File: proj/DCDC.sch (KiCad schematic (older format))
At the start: 49 parts, among them Q13 MMBT3904, Q15 MMBT3904, Q16 MMBT3904, Q17 PZT2907A, Q18 PZT2907A, Q19 MMBT3904, U14 L78M05CDT, U15 MC79M05CDT, U16 AZ1117CH-1.8TRG1, U17 MCP1700T-vv02E/TT

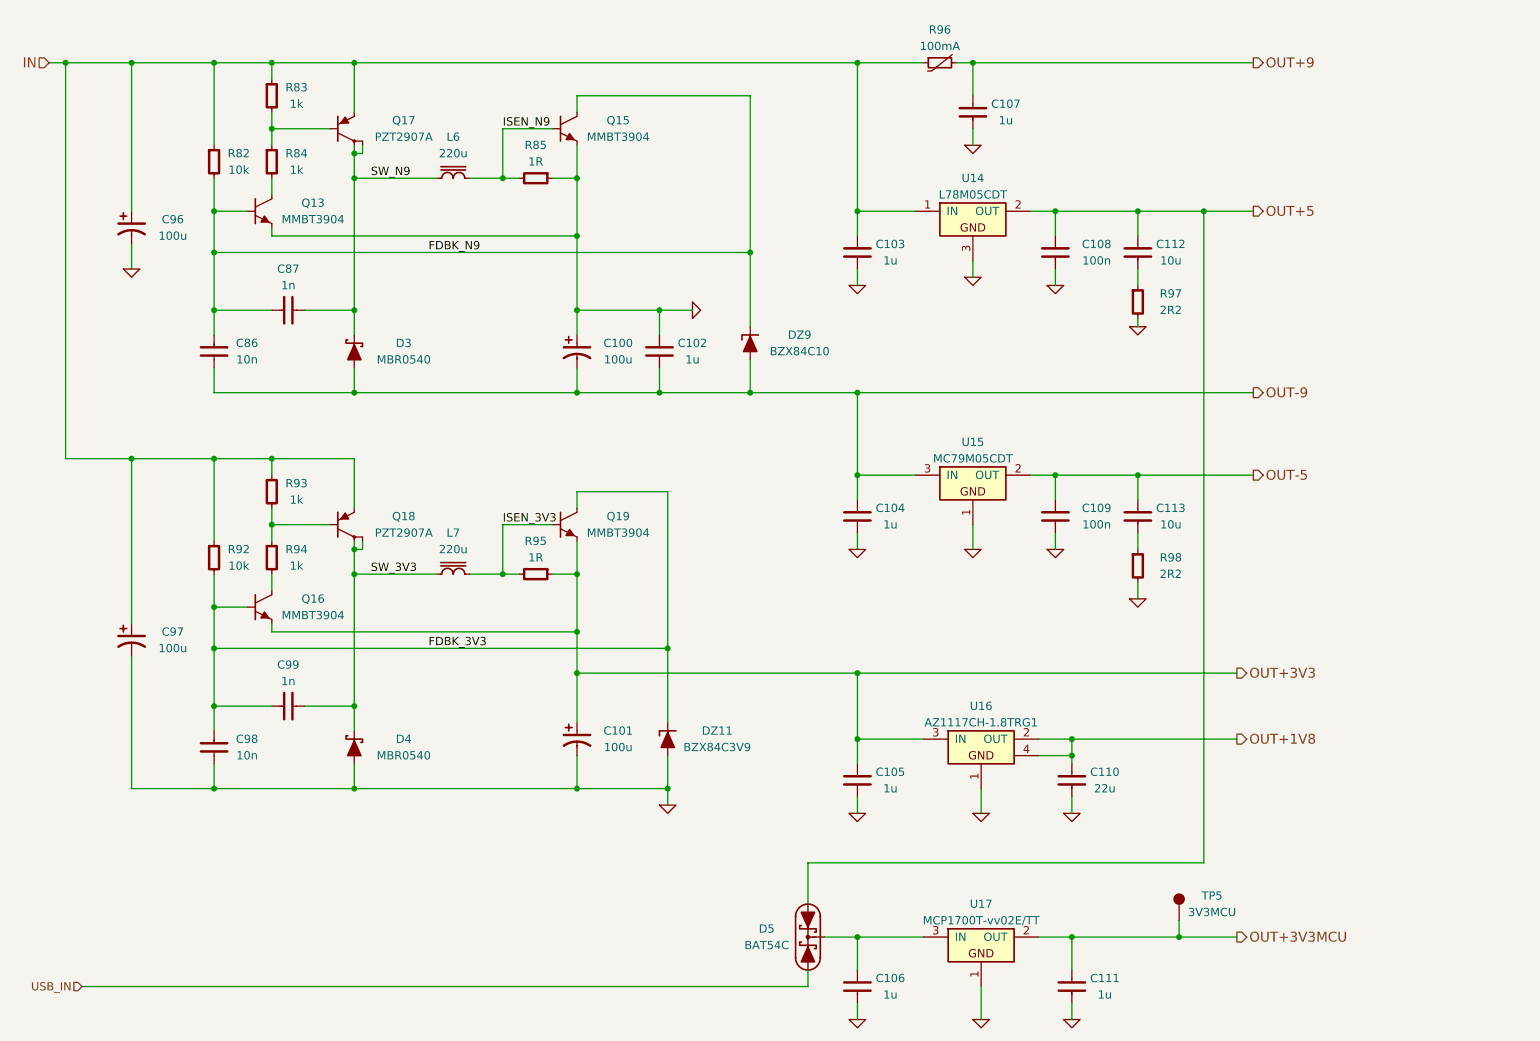
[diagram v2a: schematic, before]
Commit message: Add overload protection to aux power output
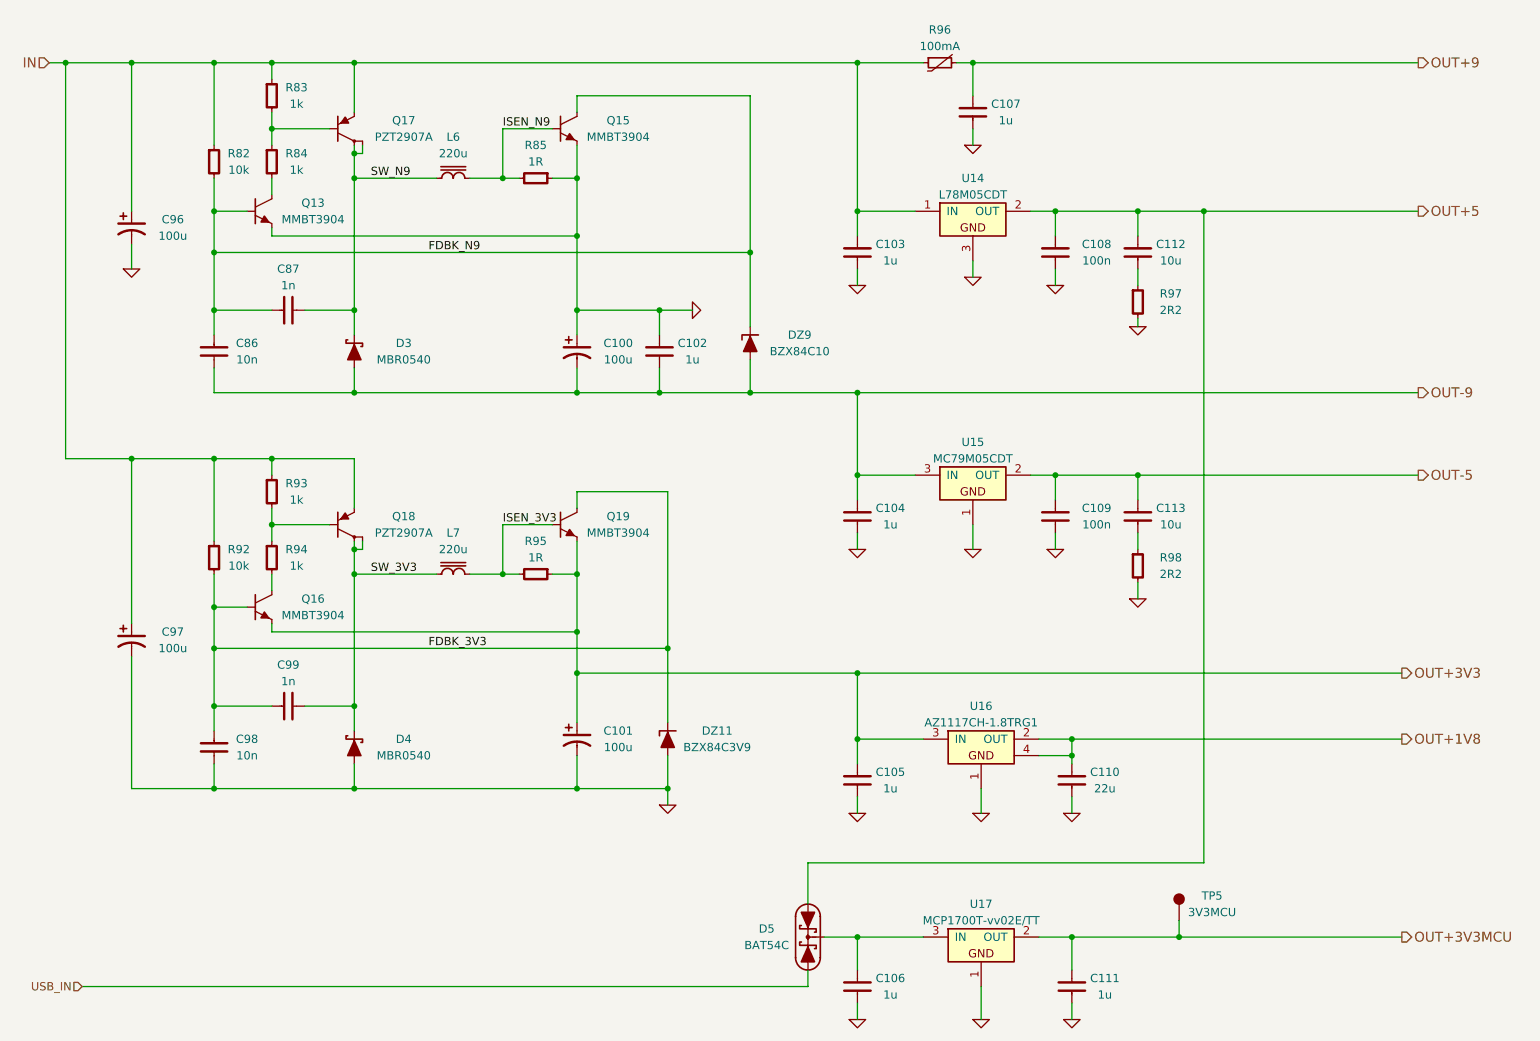
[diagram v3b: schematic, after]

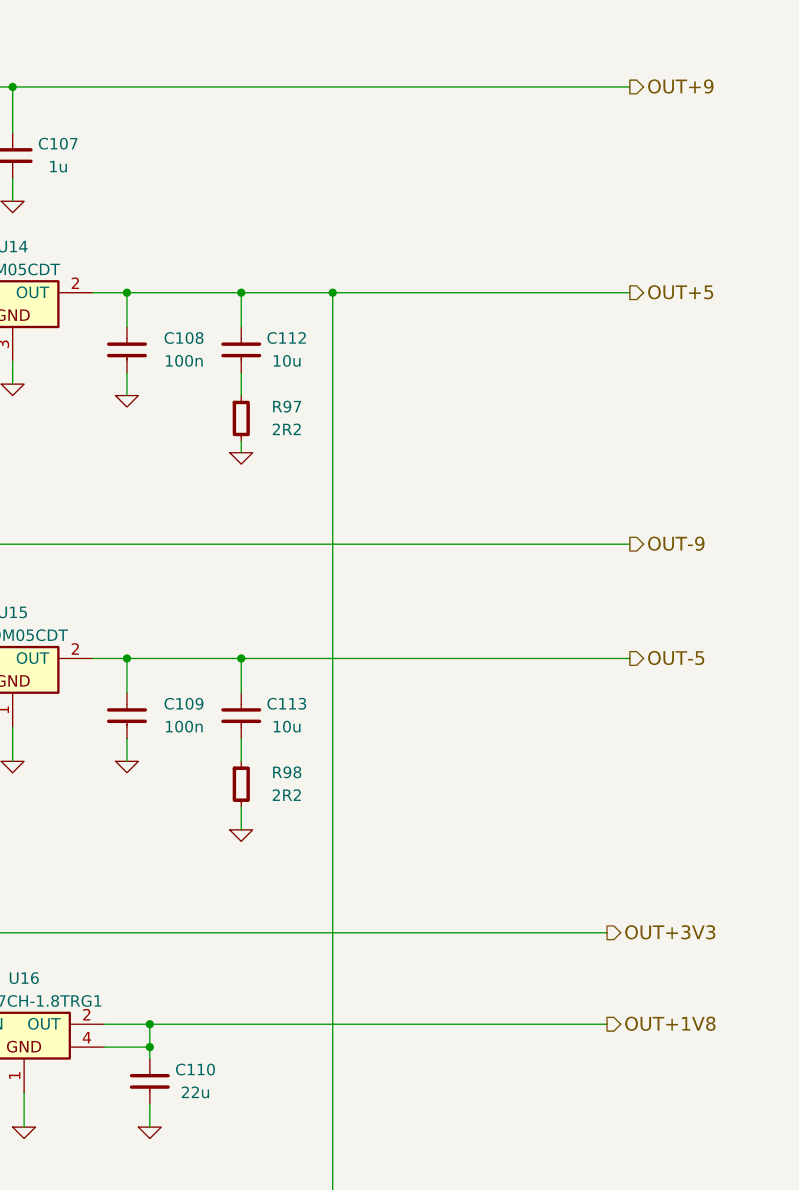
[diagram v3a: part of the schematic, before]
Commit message: Add some test points
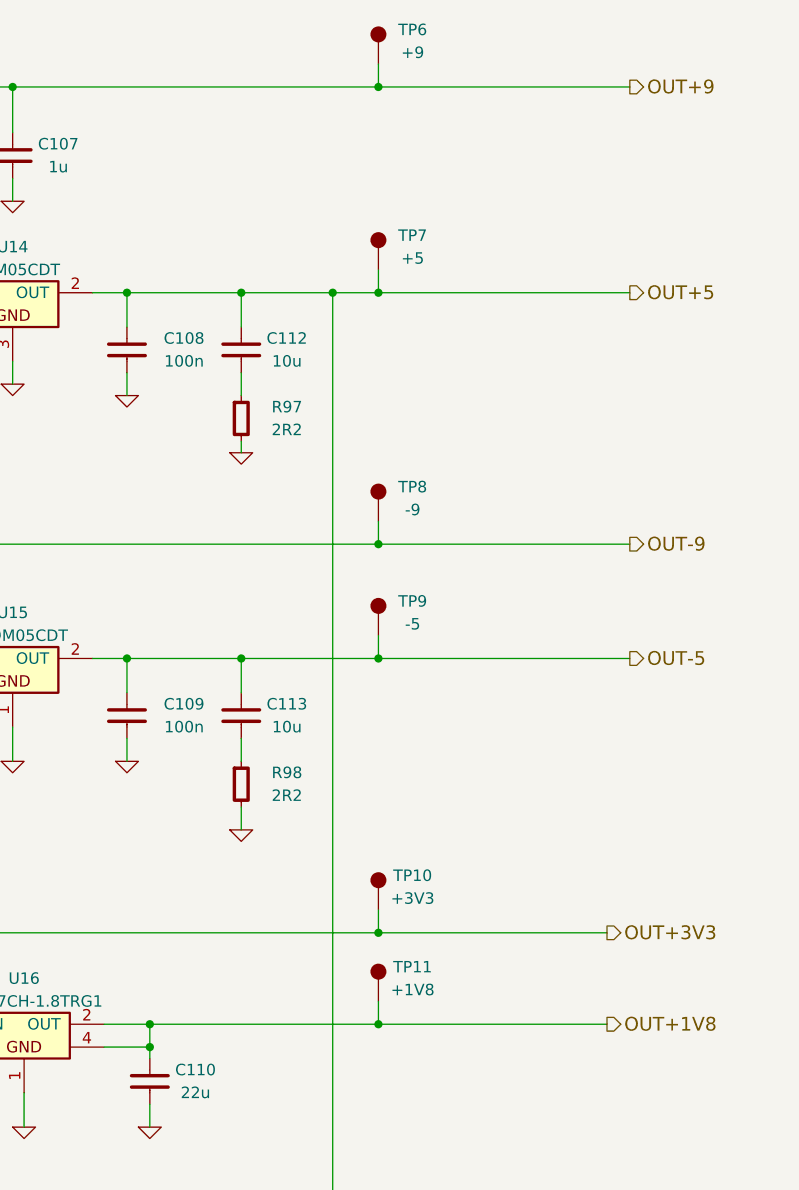
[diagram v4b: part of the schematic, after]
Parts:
- added TP10: +3V3, conn-test:TEST-SMD-SMALL, symbol TESTPOINT
- added TP11: +1V8, conn-test:TEST-SMD-SMALL, symbol TESTPOINT
- added TP6: +9, conn-test:TEST-SMD-SMALL, symbol TESTPOINT
- added TP7: +5, conn-test:TEST-SMD-SMALL, symbol TESTPOINT
- added TP8: -9, conn-test:TEST-SMD-SMALL, symbol TESTPOINT
- added TP9: -5, conn-test:TEST-SMD-SMALL, symbol TESTPOINT
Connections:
- net OUT+1V8: now also TP11.1
- net OUT+3V3: now also TP10.1
- net OUT+5: now also TP7.1
- net OUT+9: now also TP6.1
- net OUT-5: now also TP9.1
- net OUT-9: now also TP8.1
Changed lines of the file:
@@
 	10150 6100 10150 6200
 Connection ~ 10150 6200
+$Comp
+L TESTPOINT TP6
+U 1 1 54FC93D5
+P 10500 800
+F 0 "TP6" H 10650 950 50  0000 C CNN
+F 1 "+9" H 10650 850 50  0000 C CNN
+F 2 "conn-test:TEST-SMD-SMALL" H 10500 800 50  0001 C CNN
+F 3 "" H 10500 800 50  0000 C CNN
+	1    10500 800
+	1    0    0    -1
+$EndComp
+Wire Wire Line
+	10500 800  10500 900
+Connection ~ 10500 900
+$Comp
+L TESTPOINT TP7
+U 1 1 54FC99F8
+P 10500 1700
+F 0 "TP7" H 10650 1850 50  0000 C CNN
+F 1 "+5" H 10650 1750 50  0000 C CNN
+F 2 "conn-test:TEST-SMD-SMALL" H 10500 1700 50  0001 C CNN
+F 3 "" H 10500 1700 50  0000 C CNN
+	1    10500 1700
+	1    0    0    -1
+$EndComp
+Wire Wire Line
+	10500 1700 10500 1800
+Connection ~ 10500 1800
+$Comp
+L TESTPOINT TP8
+U 1 1 54FC9BF2
+P 10500 2800
+F 0 "TP8" H 10650 2950 50  0000 C CNN
+F 1 "-9" H 10650 2850 50  0000 C CNN
+F 2 "conn-test:TEST-SMD-SMALL" H 10500 2800 50  0001 C CNN
+F 3 "" H 10500 2800 50  0000 C CNN
+	1    10500 2800
+	1    0    0    -1
+$EndComp
+Wire Wire Line
+	10500 2800 10500 2900
+Connection ~ 10500 2900
+$Comp
+L TESTPOINT TP9
+U 1 1 54FC9EAA
+P 10500 3300
+F 0 "TP9" H 10650 3450 50  0000 C CNN
+F 1 "-5" H 10650 3350 50  0000 C CNN
+F 2 "conn-test:TEST-SMD-SMALL" H 10500 3300 50  0001 C CNN
+F 3 "" H 10500 3300 50  0000 C CNN
+	1    10500 3300
+	1    0    0    -1
+$EndComp
+Wire Wire Line
+	10500 3300 10500 3400
+Connection ~ 10500 3400
+$Comp
+L TESTPOINT TP10
+U 1 1 54FCA098
+P 10500 4500
+F 0 "TP10" H 10650 4650 50  0000 C CNN
+F 1 "+3V3" H 10650 4550 50  0000 C CNN
+F 2 "conn-test:TEST-SMD-SMALL" H 10500 4500 50  0001 C CNN
+F 3 "" H 10500 4500 50  0000 C CNN
+	1    10500 4500
+	1    0    0    -1
+$EndComp
+Wire Wire Line
+	10500 4500 10500 4600
+Connection ~ 10500 4600
+$Comp
+L TESTPOINT TP11
+U 1 1 54FCA29B
+P 10500 4900
+F 0 "TP11" H 10650 5050 50  0000 C CNN
+F 1 "+1V8" H 10650 4950 50  0000 C CNN
+F 2 "conn-test:TEST-SMD-SMALL" H 10500 4900 50  0001 C CNN
+F 3 "" H 10500 4900 50  0000 C CNN
+	1    10500 4900
+	1    0    0    -1
+$EndComp
+Wire Wire Line
+	10500 4900 10500 5000
+Connection ~ 10500 5000
 $EndSCHEMATC
